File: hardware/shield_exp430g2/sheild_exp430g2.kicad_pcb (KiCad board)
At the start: 2 copper layers, 57.7 x 51.3 mm, 49 parts, among them J1 Digital, J10 Conn_01x02_Male, J11 Conn_01x02_Male, J12 Conn_01x02_Male, J13 Conn_01x02_Male, J14 Conn_01x04_Male, J15 Conn_01x02_Male, J16 Conn_01x02_Male, J17 Conn_01x02_Male, J18 Conn_01x02_Male, J19 Conn_01x02_Male, J2 Digital, J20 Conn_01x02_Male, J21 Conn_01x02_Male, J22 Conn_01x02_Male, J23 Conn_01x02_Male, J24 Conn_01x02_Male, J3 Conn_01x02_Male, J4 Conn_01x02_Male, J5 Conn_01x02_Male, J6 Conn_01x02_Male, J7 Conn_01x02_Male, J8 Conn_01x02_Male, J9 Conn_02x13_Odd_Even, Q1 2N7002, Q2 2N7002, U1 NCP1117-3.3_SOT223

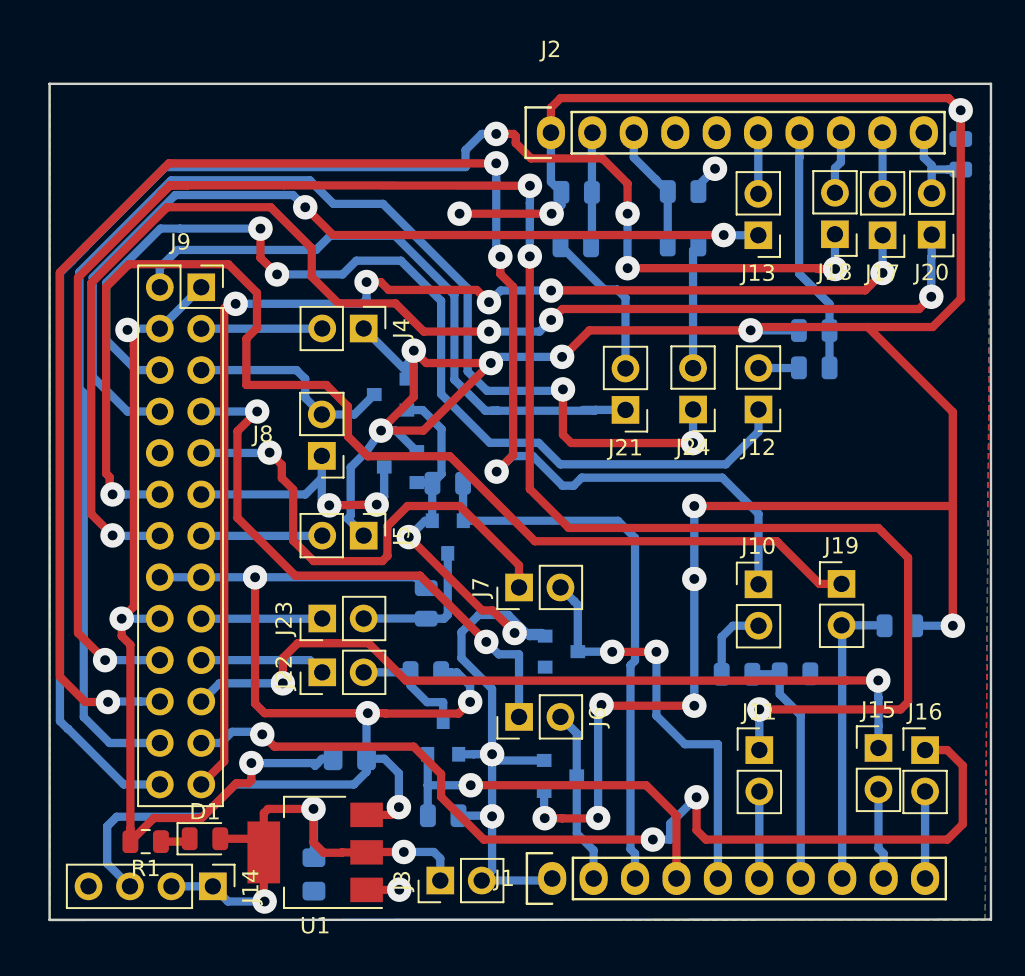
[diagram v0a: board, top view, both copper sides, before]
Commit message: Increased GND copper
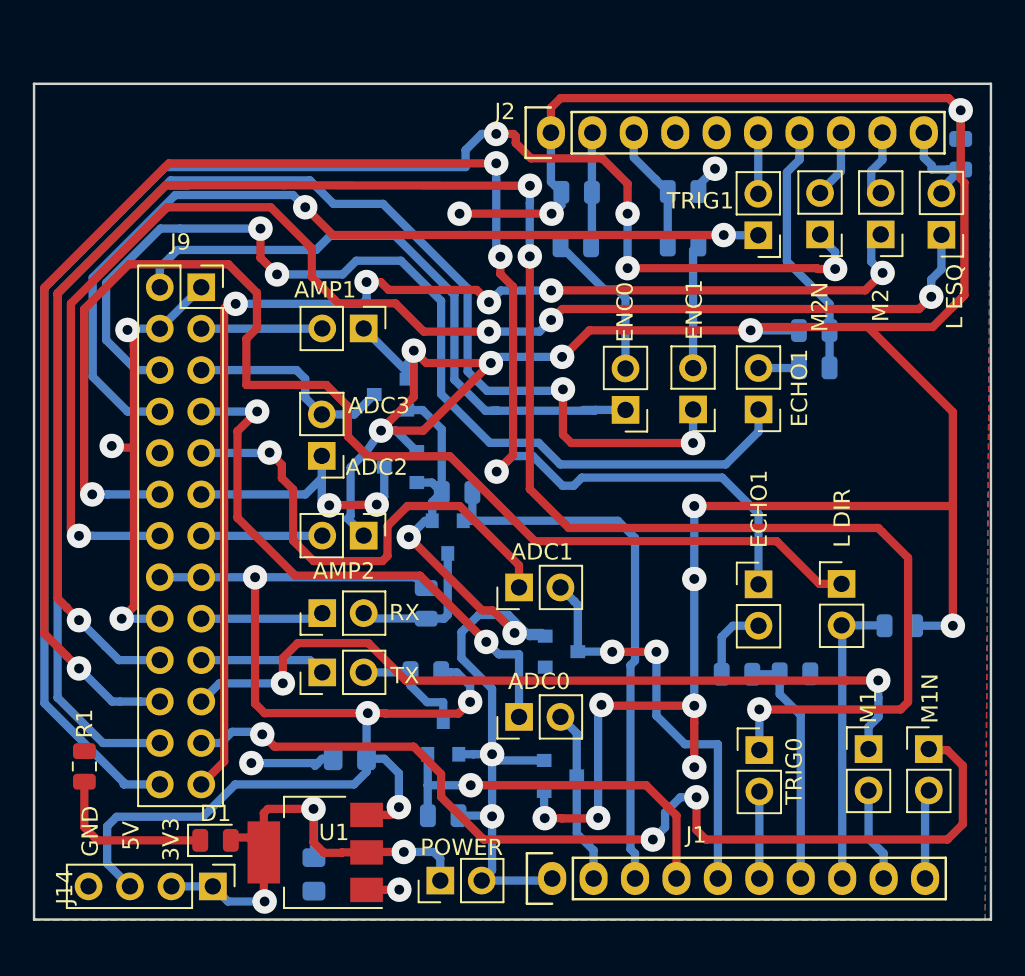
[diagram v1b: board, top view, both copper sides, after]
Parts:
- L DIR: renamed from J19
- L ESQ: renamed from J20
- moved R1 5.95 mm to (112.8, 117.0), turned to 90 degrees
- moved M2N 0.91 mm to (157.9, 84.3)
- moved R14 0.80 mm to (135.6, 100.2)
- moved D1 0.66 mm to (120.8, 121.5)
- moved M1 0.61 mm to (160.9, 115.9)
- moved L ESQ 0.60 mm to (165.3, 84.4)
- moved RX 0.33 mm to (127.4, 107.6)
- moved M1N 0.24 mm to (164.6, 115.9)
- moved M2 0.13 mm to (161.6, 84.3)
- renumbered J6 to ADC0, J7 to ADC1, J8 to ADC3, J4 to AMP1, J5 to AMP2, J12 to ECHO1, J10 to ECHO1, J21 to ENC0, J24 to ENC1, J15 to M1, J16 to M1N, J17 to M2, J18 to M2N, J3 to POWER, J23 to RX, J11 to TRIG0, J13 to TRIG1, J22 to TX
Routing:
- net GND: track 249.6 -> 231.8 mm, vias 20 -> 22
- net Net-(D1-Pad1): track 1.84 -> 10.2 mm
- net L_TCRT: track 81.2 -> 84.5 mm
- net D1: track 86.1 -> 87.5 mm
- net R_TCRT: track 75.6 -> 76.8 mm
- net +3V3: track 56.4 -> 57.2 mm
- net P1.6: track 15.2 -> 15.9 mm
- net P2.1: track 5.59 -> 6.23 mm
- net Net-(C2-Pad1): track 32.3 -> 32.9 mm
- net Echo0: track 102.8 -> 103.3 mm
- net P2.3: track 5.69 -> 6.19 mm
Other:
- board size 57.7 x 51.3 mm -> 58.7 x 51.2 mm
- board text added: "3V3"
- board text added: "5V"
- board text added: "ADC2"
- board text added: "GND"

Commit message: Otimized some tracks
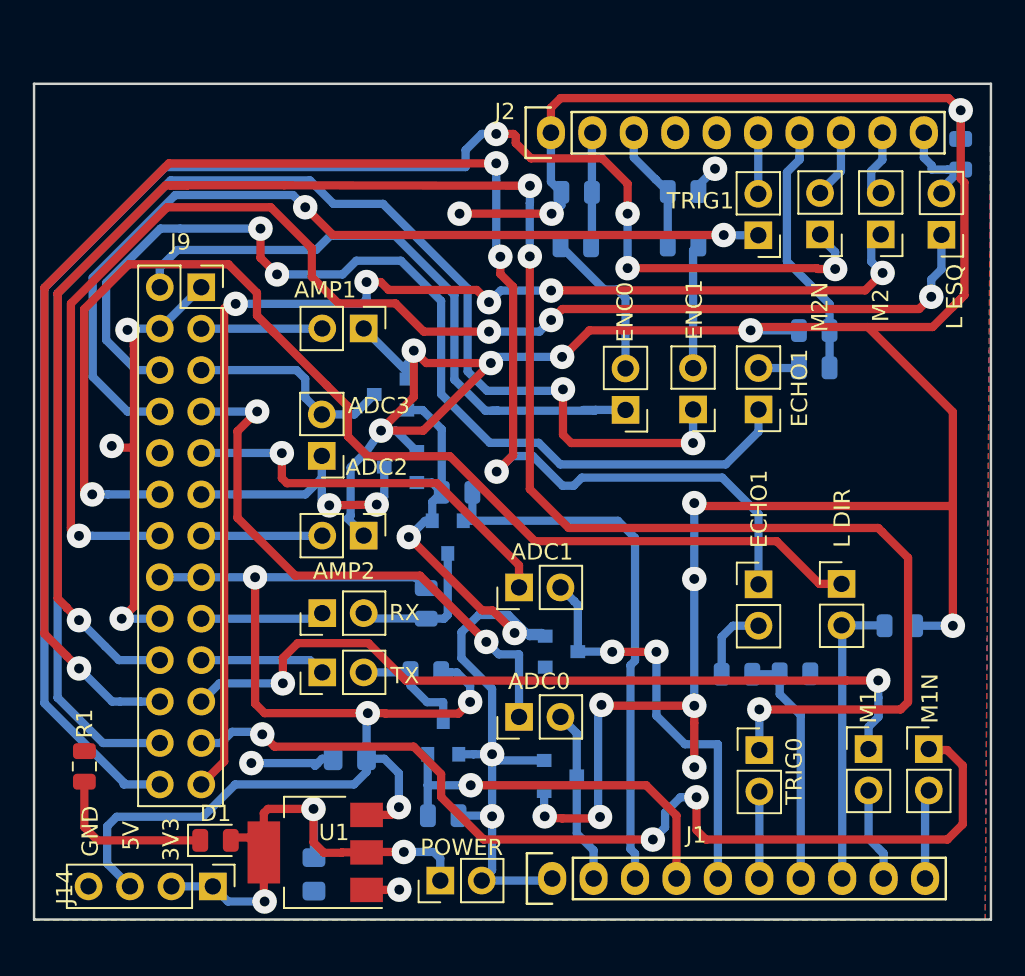
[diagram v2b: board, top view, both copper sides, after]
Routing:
- net ADC1: track 29.9 -> 23.9 mm
- net R_TCRT: track 76.8 -> 73.9 mm
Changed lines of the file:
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@@
     (thickness 1.6)
     (drawings 11)
-    (tracks 650)
+    (tracks 644)
     (zones 0)
     (modules 49)
@@
   (segment (start 166.0398 100.9904) (end 166.0398 108.331) (width 0.508) (layer F.Cu) (net 2))
   (segment (start 166.0398 95.2246) (end 166.0398 100.9904) (width 0.508) (layer F.Cu) (net 2))
-  (via (at 150.1902 100.9904) (size 1.5) (drill 0.6) (layers F.Cu B.Cu) (net 2))
+  (via (at 150.1902 100.8126) (size 1.5) (drill 0.6) (layers F.Cu B.Cu) (net 2))
   (segment (start 150.1902 100.9904) (end 150.1902 105.4608) (width 0.508) (layer B.Cu) (net 2))
   (via (at 150.1902 105.4608) (size 1.5) (drill 0.6) (layers F.Cu B.Cu) (net 2))
@@
   (segment (start 150.1902 113.2332) (end 144.5514 113.2332) (width 0.508) (layer F.Cu) (net 2))
   (segment (start 144.5514 113.2332) (end 144.5006 113.1824) (width 0.508) (layer F.Cu) (net 2))
-  (via (at 141.0208 120.1286) (size 1.5) (drill 0.6) (layers F.Cu B.Cu) (net 2))
+  (via (at 141.0208 120.015) (size 1.5) (drill 0.6) (layers F.Cu B.Cu) (net 2))
   (segment (start 140.986 118.4885) (end 140.986 120.0938) (width 0.508) (layer B.Cu) (net 2))
   (segment (start 140.986 120.0938) (end 141.0208 120.1286) (width 0.508) (layer B.Cu) (net 2))
   (segment (start 142.08146 120.1286) (end 142.09486 120.142) (width 0.508) (layer F.Cu) (net 2))
   (segment (start 141.0208 120.1286) (end 142.08146 120.1286) (width 0.508) (layer F.Cu) (net 2))
-  (via (at 144.2948 120.111477) (size 1.5) (drill 0.6) (layers F.Cu B.Cu) (net 2))
+  (via (at 144.4117 120.0531) (size 1.5) (drill 0.6) (layers F.Cu B.Cu) (net 2))
   (segment (start 142.09486 120.142) (end 144.264277 120.142) (width 0.508) (layer F.Cu) (net 2))
   (segment (start 144.264277 120.142) (end 144.2948 120.111477) (width 0.508) (layer F.Cu) (net 2))
@@
   (segment (start 118.370913 81.927001) (end 113.3094 86.988514) (width 0.508) (layer B.Cu) (net 10))
   (segment (start 125.589601 81.927001) (end 118.370913 81.927001) (width 0.508) (layer B.Cu) (net 10))
-  (via (at 124.1552 97.7138) (size 1.5) (drill 0.6) (layers F.Cu B.Cu) (net 11))
-  (segment (start 124.1298 97.7392) (end 124.1552 97.7138) (width 0.508) (layer B.Cu) (net 11))
-  (segment (start 119.9642 97.7392) (end 124.1298 97.7392) (width 0.508) (layer B.Cu) (net 11))
+  (via (at 124.9045 97.7519) (size 1.5) (drill 0.6) (layers F.Cu B.Cu) (net 11))
+  (segment (start 124.8918 97.7392) (end 124.9045 97.7519) (width 0.508) (layer B.Cu) (net 11))
+  (segment (start 119.9642 97.7392) (end 124.8918 97.7392) (width 0.508) (layer B.Cu) (net 11))
+  (segment (start 134.415397 99.592897) (end 139.446 104.6235) (width 0.508) (layer F.Cu) (net 11))
+  (segment (start 125.221497 99.592897) (end 134.415397 99.592897) (width 0.508) (layer F.Cu) (net 11))
+  (segment (start 124.905199 98.463799) (end 124.905199 99.276599) (width 0.508) (layer F.Cu) (net 11))
   (segment (start 139.446 104.6235) (end 139.446 105.9815) (width 0.508) (layer F.Cu) (net 11))
-  (segment (start 132.6134 100.9904) (end 135.8129 100.9904) (width 0.508) (layer F.Cu) (net 11))
-  (segment (start 131.380799 102.223001) (end 132.6134 100.9904) (width 0.508) (layer F.Cu) (net 11))
-  (segment (start 131.064742 104.3686) (end 131.380799 104.052543) (width 0.508) (layer F.Cu) (net 11))
-  (segment (start 131.380799 104.052543) (end 131.380799 102.223001) (width 0.508) (layer F.Cu) (net 11))
-  (segment (start 124.905199 98.463799) (end 124.905199 99.276599) (width 0.508) (layer F.Cu) (net 11))
-  (segment (start 124.1552 97.7138) (end 124.905199 98.463799) (width 0.508) (layer F.Cu) (net 11))
-  (segment (start 125.603 103.113526) (end 126.858074 104.3686) (width 0.508) (layer F.Cu) (net 11))
-  (segment (start 135.8129 100.9904) (end 139.446 104.6235) (width 0.508) (layer F.Cu) (net 11))
-  (segment (start 124.905199 99.276599) (end 125.603 99.9744) (width 0.508) (layer F.Cu) (net 11))
-  (segment (start 125.603 99.9744) (end 125.603 103.113526) (width 0.508) (layer F.Cu) (net 11))
-  (segment (start 126.858074 104.3686) (end 131.064742 104.3686) (width 0.508) (layer F.Cu) (net 11))
+  (segment (start 124.905199 99.276599) (end 125.221497 99.592897) (width 0.508) (layer F.Cu) (net 11))
   (segment (start 127.3556 99.275) (end 127.3556 97.917) (width 0.508) (layer B.Cu) (net 13))
   (segment (start 126.3514 100.2792) (end 127.3556 99.275) (width 0.508) (layer B.Cu) (net 13))
@@
   (segment (start 155.2457 103.1494) (end 157.8619 105.7656) (width 0.508) (layer F.Cu) (net 14))
   (segment (start 121.630201 86.170399) (end 123.381201 87.921399) (width 0.508) (layer F.Cu) (net 14))
-  (segment (start 122.730574 90.731026) (end 122.730574 93.571374) (width 0.508) (layer F.Cu) (net 14))
   (segment (start 112.78754 88.91386) (end 115.531001 86.170399) (width 0.508) (layer F.Cu) (net 14))
   (segment (start 128.9558 96.7232) (end 130.175 97.9424) (width 0.508) (layer F.Cu) (net 14))
   (segment (start 115.531001 86.170399) (end 121.630201 86.170399) (width 0.508) (layer F.Cu) (net 14))
   (segment (start 113.0427 100.2792) (end 112.78754 100.02404) (width 0.508) (layer F.Cu) (net 14))
-  (segment (start 123.381201 87.921399) (end 123.381201 90.080399) (width 0.508) (layer F.Cu) (net 14))
   (segment (start 113.28353 100.2792) (end 113.0427 100.2792) (width 0.508) (layer F.Cu) (net 14))
-  (segment (start 123.381201 90.080399) (end 122.730574 90.731026) (width 0.508) (layer F.Cu) (net 14))
-  (segment (start 122.730574 93.571374) (end 127.635 93.571374) (width 0.508) (layer F.Cu) (net 14))
   (segment (start 140.417686 103.1494) (end 155.2457 103.1494) (width 0.508) (layer F.Cu) (net 14))
-  (segment (start 127.635 93.571374) (end 128.9558 94.892174) (width 0.508) (layer F.Cu) (net 14))
   (segment (start 128.9558 94.892174) (end 128.9558 96.7232) (width 0.508) (layer F.Cu) (net 14))
   (segment (start 112.78754 100.02404) (end 112.78754 88.91386) (width 0.508) (layer F.Cu) (net 14))
   (segment (start 130.175 97.9424) (end 135.210686 97.9424) (width 0.508) (layer F.Cu) (net 14))
   (segment (start 135.210686 97.9424) (end 140.417686 103.1494) (width 0.508) (layer F.Cu) (net 14))
+  (segment (start 127.635 93.571374) (end 127.6604 93.596774) (width 0.508) (layer F.Cu) (net 14))
+  (segment (start 127.6604 93.596774) (end 128.9558 94.892174) (width 0.508) (layer F.Cu) (net 14))
+  (segment (start 123.381201 89.317575) (end 124.4219 90.358274) (width 0.508) (layer F.Cu) (net 14))
+  (segment (start 123.381201 87.921399) (end 123.381201 89.317575) (width 0.508) (layer F.Cu) (net 14))
+  (segment (start 124.144025 90.080399) (end 124.4219 90.358274) (width 0.508) (layer F.Cu) (net 14))
+  (segment (start 124.4219 90.358274) (end 127.6604 93.596774) (width 0.508) (layer F.Cu) (net 14))
   (segment (start 127.3683 102.8192) (end 127.381 102.8065) (width 0.508) (layer B.Cu) (net 15))
   (segment (start 119.9642 102.8192) (end 127.3683 102.8192) (width 0.508) (layer B.Cu) (net 15))
